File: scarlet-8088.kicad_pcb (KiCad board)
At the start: 2 copper layers, 0 parts

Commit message: Add grounded Mounting Holes to schematic
Signed-off-by: Lucy Mielke <user@domain.tld>
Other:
- board outline added: 305 x 244 mm
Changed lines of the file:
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@@
 		(legacy_teardrops no)
 	)
-	(paper "A4")
+	(paper "A2")
+	(title_block
+		(title "${TITLE}")
+		(date "${DATE}")
+		(rev "${REVISION}")
+		(company "${AUTHOR}")
+		(comment 1 "${COMMENT1}")
+	)
 	(layers
 		(0 "F.Cu" signal)
@@
 		(capping no)
 		(filling no)
-		(zone_defaults)
 		(pcbplotparams
 			(layerselection 0x00000000_00000000_55555555_5755f5ff)
@@
 		)
 	)
+	(property "AUTHOR" "Red Lucy Engineering")
+	(property "COMMENT1" "https://engineering.redlucy404.de")
+	(property "DATE" "${CURRENT_DATE}")
+	(property "REVISION" "1.0")
+	(property "TITLE" "\"scarlet-8088\" Intel-8088-based ATX Motherboard")
+	(gr_line
+		(start 147 99.5)
+		(end 147 343.5)
+		(stroke
+			(width 0.05)
+			(type default)
+		)
+		(layer "Edge.Cuts")
+	)
+	(gr_line
+		(start 147 99.5)
+		(end 452 99.5)
+		(stroke
+			(width 0.05)
+			(type default)
+		)
+		(layer "Edge.Cuts")
+	)
+	(gr_line
+		(start 147 343.5)
+		(end 452 343.5)
+		(stroke
+			(width 0.05)
+			(type default)
+		)
+		(layer "Edge.Cuts")
+	)
+	(gr_line
+		(start 452 343.5)
+		(end 452 99.5)
+		(stroke
+			(width 0.05)
+			(type default)
+		)
+		(layer "Edge.Cuts")
+	)
 	(embedded_fonts no)

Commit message: setup for JLCPCB 4-Layers
Signed-off-by: Lucy Mielke <user@domain.tld>
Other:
- copper layers 2 -> 4
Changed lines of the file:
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@@
 	(generator_version "10.0")
 	(general
-		(thickness 1.6)
+		(thickness 1.600198)
 		(legacy_teardrops no)
 	)
@@
 	)
 	(layers
-		(0 "F.Cu" signal)
-		(2 "B.Cu" signal)
-		(9 "F.Adhes" user "F.Adhesive")
-		(11 "B.Adhes" user "B.Adhesive")
+		(0 "F.Cu" signal "Front")
+		(4 "In1.Cu" signal)
+		(6 "In2.Cu" signal)
+		(2 "B.Cu" signal "Back")
 		(13 "F.Paste" user)
 		(15 "B.Paste" user)
-		(5 "F.SilkS" user "F.Silkscreen")
-		(7 "B.SilkS" user "B.Silkscreen")
+		(5 "F.SilkS" user)
+		(7 "B.SilkS" user)
 		(1 "F.Mask" user)
 		(3 "B.Mask" user)
-		(17 "Dwgs.User" user "User.Drawings")
-		(19 "Cmts.User" user "User.Comments")
-		(21 "Eco1.User" user "User.Eco1")
-		(23 "Eco2.User" user "User.Eco2")
 		(25 "Edge.Cuts" user)
 		(27 "Margin" user)
-		(31 "F.CrtYd" user "F.Courtyard")
-		(29 "B.CrtYd" user "B.Courtyard")
+		(31 "F.CrtYd" user)
+		(29 "B.CrtYd" user)
 		(35 "F.Fab" user)
-		(33 "B.Fab" user)
-		(39 "User.1" user)
-		(41 "User.2" user)
-		(43 "User.3" user)
-		(45 "User.4" user)
 	)
 	(setup
@@
 			(layer "dielectric 1"
 				(type "core")
-				(thickness 1.51)
+				(thickness 0.480066)
+				(material "FR4")
+				(epsilon_r 4.5)
+				(loss_tangent 0.02)
+			)
+			(layer "In1.Cu"
+				(type "copper")
+				(thickness 0.035)
+			)
+			(layer "dielectric 2"
+				(type "prepreg")
+				(thickness 0.480066)
+				(material "FR4")
+				(epsilon_r 4.5)
+				(loss_tangent 0.02)
+			)
+			(layer "In2.Cu"
+				(type "copper")
+				(thickness 0.035)
+			)
+			(layer "dielectric 3"
+				(type "core")
+				(thickness 0.480066)
 				(material "FR4")
 				(epsilon_r 4.5)
@@
 		)
 		(pad_to_mask_clearance 0)
+		(solder_mask_min_width 0.1016)
 		(allow_soldermask_bridges_in_footprints no)
 		(tenting
@@
 		(capping no)
 		(filling no)
+		(zone_defaults)
 		(pcbplotparams
 			(layerselection 0x00000000_00000000_55555555_5755f5ff)

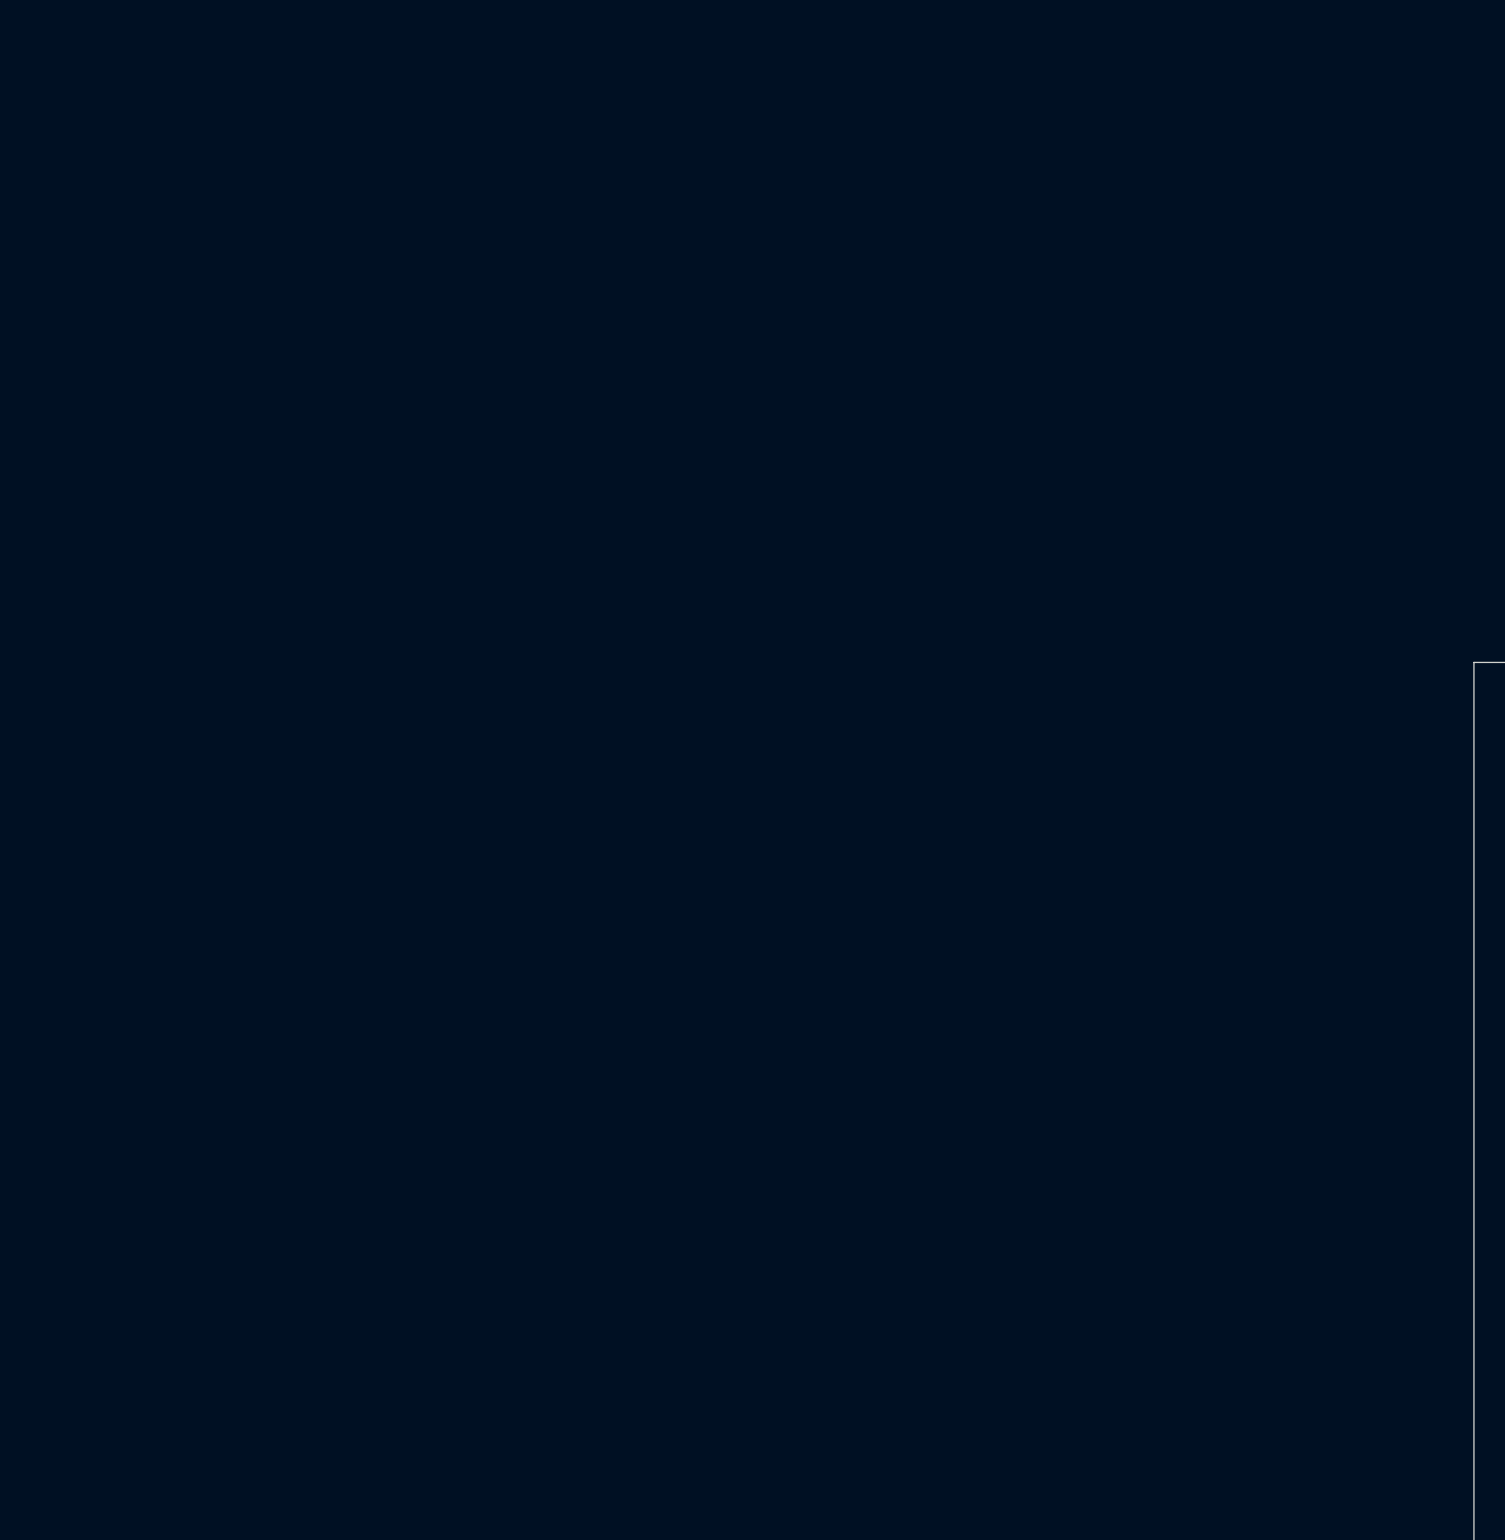
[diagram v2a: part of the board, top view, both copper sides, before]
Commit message: import all components into PCB editor
Signed-off-by: Lucy Mielke <user@domain.tld>
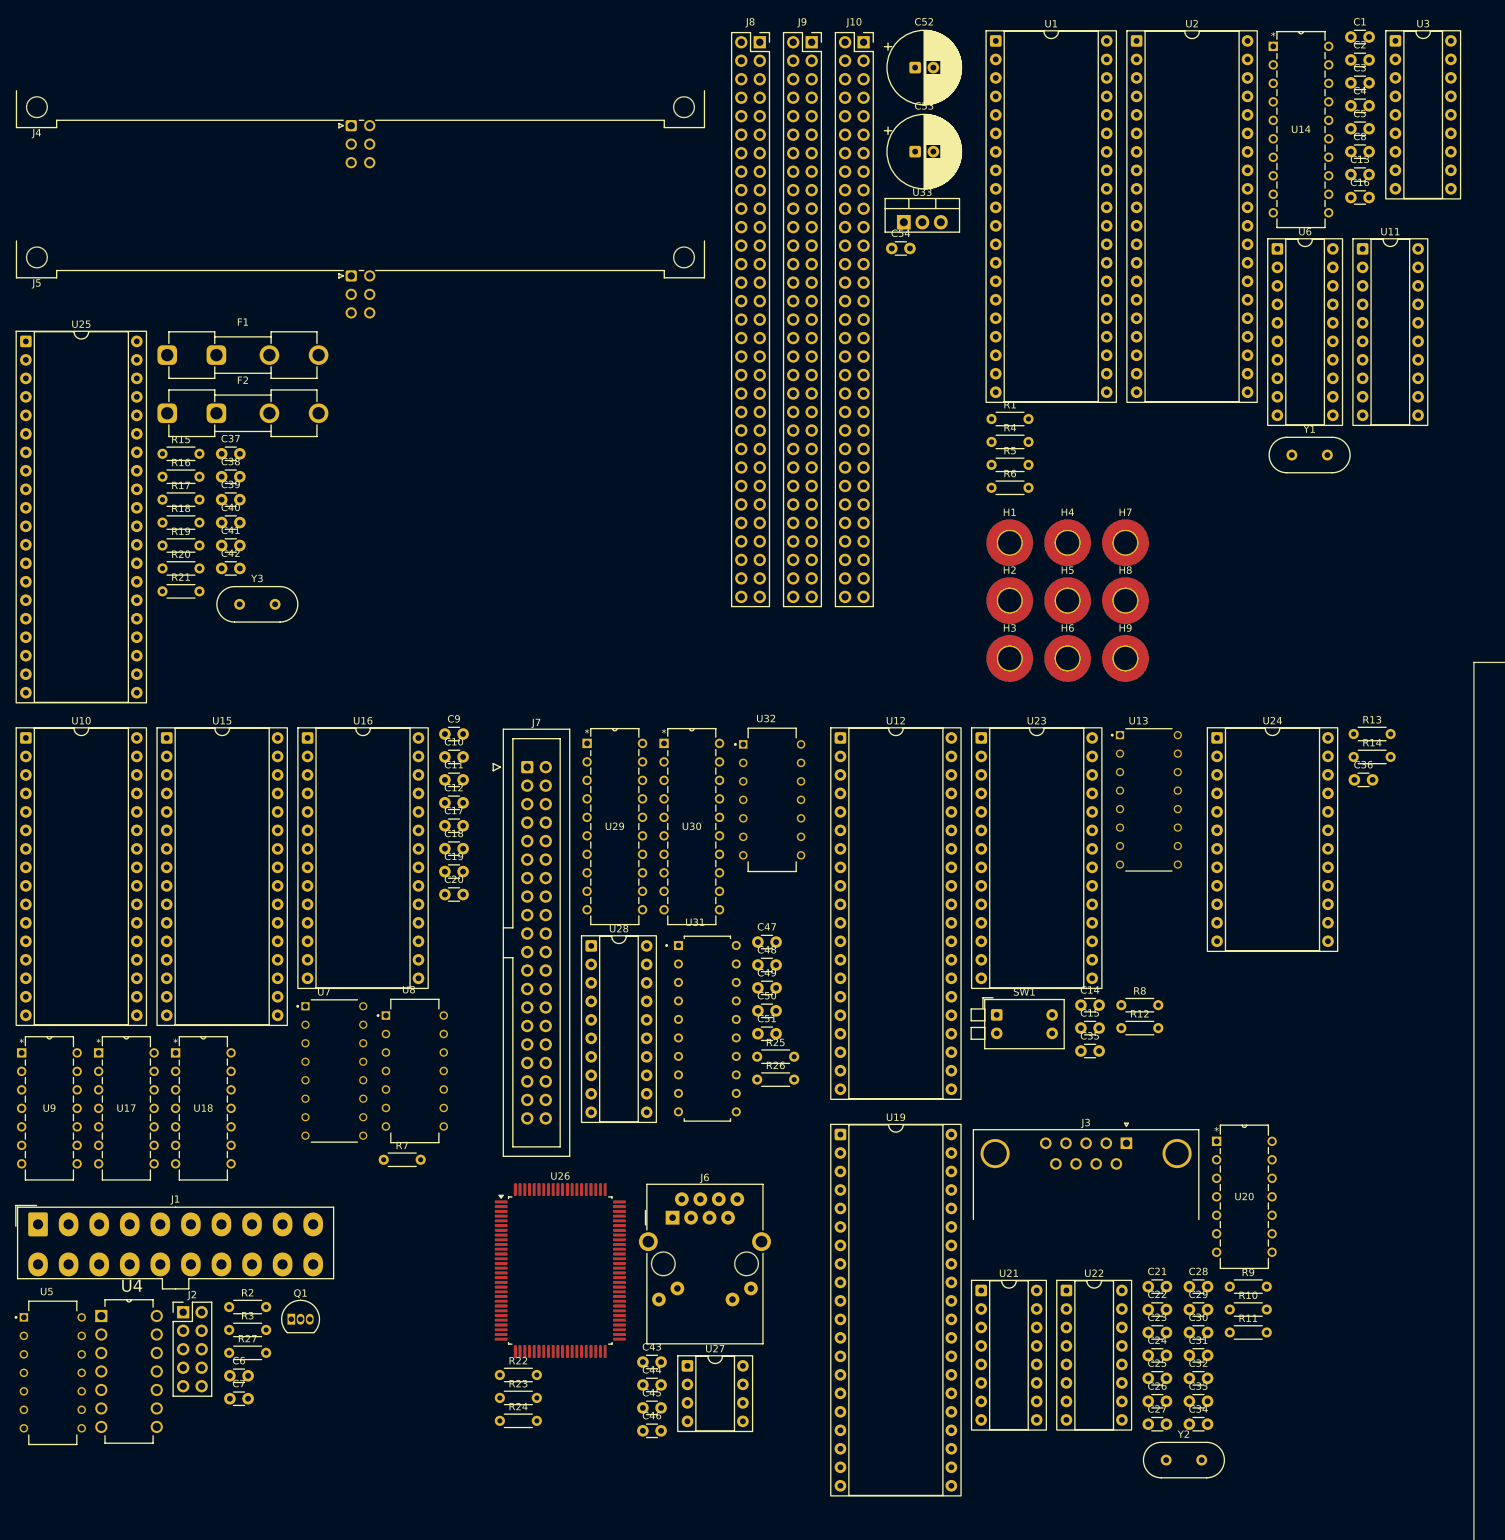
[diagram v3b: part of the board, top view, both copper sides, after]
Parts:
- added C1: 0.1uF, Capacitor_THT:C_Disc_D3.0mm_W1.6mm_P2.50mm, F.Cu at (130.1, 13.6)
- added C10: 0.1uF, Capacitor_THT:C_Disc_D3.0mm_W1.6mm_P2.50mm, F.Cu at (5.62, 112.5)
- added C11: 0.1uF, Capacitor_THT:C_Disc_D3.0mm_W1.6mm_P2.50mm, F.Cu at (5.62, 115.6)
- added C12: 0.1uF, Capacitor_THT:C_Disc_D3.0mm_W1.6mm_P2.50mm, F.Cu at (5.62, 118.8)
- added C13: 0.1uF, Capacitor_THT:C_Disc_D3.0mm_W1.6mm_P2.50mm, F.Cu at (130.1, 32.5)
- added C14: 0.1uF, Capacitor_THT:C_Disc_D3.0mm_W1.6mm_P2.50mm, F.Cu at (93.0, 146.6)
- added C15: 0.1uF, Capacitor_THT:C_Disc_D3.0mm_W1.6mm_P2.50mm, F.Cu at (93.0, 149.7)
- added C16: 0.1uF, Capacitor_THT:C_Disc_D3.0mm_W1.6mm_P2.50mm, F.Cu at (130.1, 35.6)
- added C17: 0.1uF, Capacitor_THT:C_Disc_D3.0mm_W1.6mm_P2.50mm, F.Cu at (5.62, 121.9)
- added C18: 0.1uF, Capacitor_THT:C_Disc_D3.0mm_W1.6mm_P2.50mm, F.Cu at (5.62, 125.1)
- added C19: 0.1uF, Capacitor_THT:C_Disc_D3.0mm_W1.6mm_P2.50mm, F.Cu at (5.62, 128.2)
- added C2: 0.1uF, Capacitor_THT:C_Disc_D3.0mm_W1.6mm_P2.50mm, F.Cu at (130.1, 16.7)
- added C20: 0.1uF, Capacitor_THT:C_Disc_D3.0mm_W1.6mm_P2.50mm, F.Cu at (5.62, 131.4)
- added C21: 0.1uF, Capacitor_THT:C_Disc_D3.0mm_W1.6mm_P2.50mm, F.Cu at (102.3, 185.3)
- added C22: 0.1uF, Capacitor_THT:C_Disc_D3.0mm_W1.6mm_P2.50mm, F.Cu at (102.3, 188.4)
- added C23: 20pF, Capacitor_THT:C_Disc_D3.0mm_W1.6mm_P2.50mm, F.Cu at (102.3, 191.6)
- added C24: 20pF, Capacitor_THT:C_Disc_D3.0mm_W1.6mm_P2.50mm, F.Cu at (102.3, 194.7)
- added C25: 0.1uF, Capacitor_THT:C_Disc_D3.0mm_W1.6mm_P2.50mm, F.Cu at (102.3, 197.9)
- added C26: 0.1uF, Capacitor_THT:C_Disc_D3.0mm_W1.6mm_P2.50mm, F.Cu at (102.3, 201.0)
- added C27: 1uF, Capacitor_THT:C_Disc_D3.0mm_W1.6mm_P2.50mm, F.Cu at (102.3, 204.2)
- added C28: 1uF, Capacitor_THT:C_Disc_D3.0mm_W1.6mm_P2.50mm, F.Cu at (107.9, 185.3)
- added C29: 1uF, Capacitor_THT:C_Disc_D3.0mm_W1.6mm_P2.50mm, F.Cu at (107.9, 188.4)
- added C3: 0.1uF, Capacitor_THT:C_Disc_D3.0mm_W1.6mm_P2.50mm, F.Cu at (130.1, 19.9)
- added C30: 1uF, Capacitor_THT:C_Disc_D3.0mm_W1.6mm_P2.50mm, F.Cu at (107.9, 191.6)
- added C31: 1uF, Capacitor_THT:C_Disc_D3.0mm_W1.6mm_P2.50mm, F.Cu at (107.9, 194.7)
- added C32: 1uF, Capacitor_THT:C_Disc_D3.0mm_W1.6mm_P2.50mm, F.Cu at (107.9, 197.9)
- added C33: 1uF, Capacitor_THT:C_Disc_D3.0mm_W1.6mm_P2.50mm, F.Cu at (107.9, 201.0)
- added C34: 1uF, Capacitor_THT:C_Disc_D3.0mm_W1.6mm_P2.50mm, F.Cu at (107.9, 204.2)
- added C35: 0.1uF, Capacitor_THT:C_Disc_D3.0mm_W1.6mm_P2.50mm, F.Cu at (93.0, 152.9)
- added C36: 0.1uF, Capacitor_THT:C_Disc_D3.0mm_W1.6mm_P2.50mm, F.Cu at (130.6, 115.6)
- added C37: 0.1uF, Capacitor_THT:C_Disc_D3.0mm_W1.6mm_P2.50mm, F.Cu at (-25.0, 70.8)
- added C38: 0.1uF, Capacitor_THT:C_Disc_D3.0mm_W1.6mm_P2.50mm, F.Cu at (-25.0, 74.0)
- added C39: 20pF, Capacitor_THT:C_Disc_D3.0mm_W1.6mm_P2.50mm, F.Cu at (-25.0, 77.1)
- added C4: 20pF, Capacitor_THT:C_Disc_D3.0mm_W1.6mm_P2.50mm, F.Cu at (130.1, 23.0)
- added C40: 20pF, Capacitor_THT:C_Disc_D3.0mm_W1.6mm_P2.50mm, F.Cu at (-25.0, 80.3)
- added C41: 0.1uF, Capacitor_THT:C_Disc_D3.0mm_W1.6mm_P2.50mm, F.Cu at (-25.0, 83.4)
- added C42: 0.1uF, Capacitor_THT:C_Disc_D3.0mm_W1.6mm_P2.50mm, F.Cu at (-25.0, 86.6)
- added C43: 0.1uF, Capacitor_THT:C_Disc_D3.0mm_W1.6mm_P2.50mm, F.Cu at (32.8, 195.6)
- added C44: 0.1uF, Capacitor_THT:C_Disc_D3.0mm_W1.6mm_P2.50mm, F.Cu at (32.8, 198.8)
- added C45: 0.1uF, Capacitor_THT:C_Disc_D3.0mm_W1.6mm_P2.50mm, F.Cu at (32.8, 201.9)
- added C46: 0.1uF, Capacitor_THT:C_Disc_D3.0mm_W1.6mm_P2.50mm, F.Cu at (32.8, 205.1)
- added C47: 0.1uF, Capacitor_THT:C_Disc_D3.0mm_W1.6mm_P2.50mm, F.Cu at (48.6, 137.9)
- added C48: 0.1uF, Capacitor_THT:C_Disc_D3.0mm_W1.6mm_P2.50mm, F.Cu at (48.6, 141.1)
- added C49: 0.1uF, Capacitor_THT:C_Disc_D3.0mm_W1.6mm_P2.50mm, F.Cu at (48.6, 144.2)
- added C5: 20pF, Capacitor_THT:C_Disc_D3.0mm_W1.6mm_P2.50mm, F.Cu at (130.1, 26.2)
- added C50: 0.1uF, Capacitor_THT:C_Disc_D3.0mm_W1.6mm_P2.50mm, F.Cu at (48.6, 147.4)
- added C51: 0.1uF, Capacitor_THT:C_Disc_D3.0mm_W1.6mm_P2.50mm, F.Cu at (48.6, 150.5)
- added C52: 2.2uF, Capacitor_THT:CP_Radial_D10.0mm_P2.50mm, F.Cu at (70.2, 17.8)
- added C53: 2.2uF, Capacitor_THT:CP_Radial_D10.0mm_P2.50mm, F.Cu at (70.2, 29.3)
- added C54: 0.1uF, Capacitor_THT:C_Disc_D3.0mm_W1.6mm_P2.50mm, F.Cu at (67.0, 42.6)
- added C6: 0.1uF, Capacitor_THT:C_Disc_D3.0mm_W1.6mm_P2.50mm, F.Cu at (-23.9, 197.5)
- added C7: 0.1uF, Capacitor_THT:C_Disc_D3.0mm_W1.6mm_P2.50mm, F.Cu at (-23.9, 200.7)
- added C8: 0.1uF, Capacitor_THT:C_Disc_D3.0mm_W1.6mm_P2.50mm, F.Cu at (130.1, 29.3)
- added C9: 0.1uF, Capacitor_THT:C_Disc_D3.0mm_W1.6mm_P2.50mm, F.Cu at (5.62, 109.3)
- added F1: Fuse, Fuse:Fuseholder_Clip-5x20mm_Eaton_1A5601-01_Inline_P20.80x6.76mm_D1.70mm_Horizontal, F.Cu at (-32.5, 57.3)
- added F2: Fuse, Fuse:Fuseholder_Clip-5x20mm_Eaton_1A5601-01_Inline_P20.80x6.76mm_D1.70mm_Horizontal, F.Cu at (-32.5, 65.3)
- added H1: MountingHole_Pad, MountingHole:MountingHole_3.2mm_M3_Pad_TopBottom, F.Cu at (83.2, 83.1)
- added H2: MountingHole_Pad, MountingHole:MountingHole_3.2mm_M3_Pad_TopBottom, F.Cu at (83.2, 91.0)
- added H3: MountingHole_Pad, MountingHole:MountingHole_3.2mm_M3_Pad_TopBottom, F.Cu at (83.2, 99.0)
- added H4: MountingHole_Pad, MountingHole:MountingHole_3.2mm_M3_Pad_TopBottom, F.Cu at (91.2, 83.1)
- added H5: MountingHole_Pad, MountingHole:MountingHole_3.2mm_M3_Pad_TopBottom, F.Cu at (91.2, 91.0)
- added H6: MountingHole_Pad, MountingHole:MountingHole_3.2mm_M3_Pad_TopBottom, F.Cu at (91.2, 99.0)
- added H7: MountingHole_Pad, MountingHole:MountingHole_3.2mm_M3_Pad_TopBottom, F.Cu at (99.1, 83.1)
- added H8: MountingHole_Pad, MountingHole:MountingHole_3.2mm_M3_Pad_TopBottom, F.Cu at (99.1, 91.0)
- added H9: MountingHole_Pad, MountingHole:MountingHole_3.2mm_M3_Pad_TopBottom, F.Cu at (99.1, 99.0)
- added J1: ATX-20, Connector_Molex:Molex_Mini-Fit_Jr_5566-20A_2x10_P4.20mm_Vertical, F.Cu at (-50.3, 176.7)
- added J10: Bus_ISA_8bit, Connector_PinSocket_2.54mm:PinSocket_2x31_P2.54mm_Vertical, F.Cu at (63.1, 14.3)
- added J2: F_PANEL, Connector_PinHeader_2.54mm:PinHeader_2x05_P2.54mm_Vertical, F.Cu at (-30.3, 188.8)
- added J3: DE-9SA-J4-2R, Connector_Dsub:DSUB-9_Socket_Horizontal_P2.77x2.84mm_EdgePinOffset7.70mm_Housed_MountingHolesOffset9.12mm, F.Cu at (99.3, 165.6)
- added J4: Mini-DIN-6 KBD, Connector_DIN:DIN41612_M-invers_3x2+10_Female_Horizontal_THT, F.Cu at (-45.3, 25.8)
- added J5: Mini-DIN-6 Mouse, Connector_DIN:DIN41612_M-invers_3x2+10_Female_Horizontal_THT, F.Cu at (-45.3, 46.4)
- added J6: RJ45_Amphenol_RJMG1BD3B8K1ANR, Connector_RJ:RJ45_Amphenol_RJMG1BD3B8K1ANR, F.Cu at (36.9, 175.8)
- added J7: Conn_02x20_Odd_Even, Connector_IDC:IDC-Header_2x20_P2.54mm_Vertical, F.Cu at (16.9, 113.9)
- added J8: Bus_ISA_8bit, Connector_PinSocket_2.54mm:PinSocket_2x31_P2.54mm_Vertical, F.Cu at (48.9, 14.3)
- added J9: Bus_ISA_8bit, Connector_PinSocket_2.54mm:PinSocket_2x31_P2.54mm_Vertical, F.Cu at (56.0, 14.3)
- added Q1: 2N7000, Package_TO_SOT_THT:TO-92_Inline, F.Cu at (-15.5, 189.7)
- added R1: 10k, Resistor_THT:R_Axial_DIN0204_L3.6mm_D1.6mm_P5.08mm_Horizontal, F.Cu at (80.7, 66.1)
- added R10: 10k, Resistor_THT:R_Axial_DIN0204_L3.6mm_D1.6mm_P5.08mm_Horizontal, F.Cu at (113.5, 188.4)
- added R11: 10k, Resistor_THT:R_Axial_DIN0204_L3.6mm_D1.6mm_P5.08mm_Horizontal, F.Cu at (113.5, 191.6)
- added R12: 10k, Resistor_THT:R_Axial_DIN0204_L3.6mm_D1.6mm_P5.08mm_Horizontal, F.Cu at (98.6, 149.7)
- added R13: 10k, Resistor_THT:R_Axial_DIN0204_L3.6mm_D1.6mm_P5.08mm_Horizontal, F.Cu at (130.5, 109.3)
- added R14: 10k, Resistor_THT:R_Axial_DIN0204_L3.6mm_D1.6mm_P5.08mm_Horizontal, F.Cu at (130.5, 112.5)
- added R15: 10k, Resistor_THT:R_Axial_DIN0204_L3.6mm_D1.6mm_P5.08mm_Horizontal, F.Cu at (-33.2, 70.8)
- added R16: 10k, Resistor_THT:R_Axial_DIN0204_L3.6mm_D1.6mm_P5.08mm_Horizontal, F.Cu at (-33.2, 74.0)
- added R17: 10k, Resistor_THT:R_Axial_DIN0204_L3.6mm_D1.6mm_P5.08mm_Horizontal, F.Cu at (-33.2, 77.1)
- added R18: 4,7k, Resistor_THT:R_Axial_DIN0204_L3.6mm_D1.6mm_P5.08mm_Horizontal, F.Cu at (-33.2, 80.3)
- added R19: 4,7k, Resistor_THT:R_Axial_DIN0204_L3.6mm_D1.6mm_P5.08mm_Horizontal, F.Cu at (-33.2, 83.4)
- added R2: 10k, Resistor_THT:R_Axial_DIN0204_L3.6mm_D1.6mm_P5.08mm_Horizontal, F.Cu at (-24.0, 188.1)
- added R20: 4,7k, Resistor_THT:R_Axial_DIN0204_L3.6mm_D1.6mm_P5.08mm_Horizontal, F.Cu at (-33.2, 86.6)
- added R21: 4,7k, Resistor_THT:R_Axial_DIN0204_L3.6mm_D1.6mm_P5.08mm_Horizontal, F.Cu at (-33.2, 89.7)
- added R22: 10k, Resistor_THT:R_Axial_DIN0204_L3.6mm_D1.6mm_P5.08mm_Horizontal, F.Cu at (13.2, 197.4)
- added R23: 3,3R, Resistor_THT:R_Axial_DIN0204_L3.6mm_D1.6mm_P5.08mm_Horizontal, F.Cu at (13.2, 200.5)
- added R24: 3,3R, Resistor_THT:R_Axial_DIN0204_L3.6mm_D1.6mm_P5.08mm_Horizontal, F.Cu at (13.2, 203.7)
- added R25: 10k, Resistor_THT:R_Axial_DIN0204_L3.6mm_D1.6mm_P5.08mm_Horizontal, F.Cu at (48.5, 153.7)
- added R26: 10k, Resistor_THT:R_Axial_DIN0204_L3.6mm_D1.6mm_P5.08mm_Horizontal, F.Cu at (48.5, 156.8)
- added R27: 3,3R, Resistor_THT:R_Axial_DIN0204_L3.6mm_D1.6mm_P5.08mm_Horizontal, F.Cu at (-24.0, 194.4)
- added R3: 10k, Resistor_THT:R_Axial_DIN0204_L3.6mm_D1.6mm_P5.08mm_Horizontal, F.Cu at (-24.0, 191.2)
- added R4: 10k, Resistor_THT:R_Axial_DIN0204_L3.6mm_D1.6mm_P5.08mm_Horizontal, F.Cu at (80.7, 69.2)
- added R5: 10k, Resistor_THT:R_Axial_DIN0204_L3.6mm_D1.6mm_P5.08mm_Horizontal, F.Cu at (80.7, 72.4)
- added R6: 10k, Resistor_THT:R_Axial_DIN0204_L3.6mm_D1.6mm_P5.08mm_Horizontal, F.Cu at (80.7, 75.5)
- added R7: 10k, Resistor_THT:R_Axial_DIN0204_L3.6mm_D1.6mm_P5.08mm_Horizontal, F.Cu at (-2.79, 167.8)
- added R8: 10k, Resistor_THT:R_Axial_DIN0204_L3.6mm_D1.6mm_P5.08mm_Horizontal, F.Cu at (98.6, 146.6)
- added R9: 10k, Resistor_THT:R_Axial_DIN0204_L3.6mm_D1.6mm_P5.08mm_Horizontal, F.Cu at (113.5, 185.3)
- added SW1: SW_DIP_x08, Button_Switch_THT:SW_DIP_SPSTx02_Piano_10.8x6.64mm_W7.62mm_P2.54mm, F.Cu at (81.4, 147.9)
- added U1: Intel_8088, Package_DIP:DIP-40_W15.24mm_Socket, F.Cu at (81.3, 14.1)
- added U10: AS6C4008-55PCN, Package_DIP:DIP-32_W15.24mm_Socket, F.Cu at (-51.9, 109.9)
- added U11: 74HCT373, Package_DIP:DIP-20_W7.62mm_Socket, F.Cu at (131.7, 42.7)
- added U12: 8255A, Package_DIP:DIP-40_W15.24mm_Socket, F.Cu at (60.0, 109.9)
- added U13: SN74HCT138N, SN74HCT138N Decoder/DEMUX:DIP794W45P254L1969H508Q16, F.Cu at (102.3, 118.4)
- added U14: SN74HCT245N, SN74HCT245N Transciever:SN74HCT245N, F.Cu at (127.0, 37.7)
- added U15: AS6C4008-55PCN, Package_DIP:DIP-32_W15.24mm_Socket, F.Cu at (-32.6, 109.9)
- added U16: 28C256, Package_DIP:DIP-28_W15.24mm_Socket, F.Cu at (-13.2, 109.9)
- added U17: CD74HCT14E, CD74HCT14E Inverter:CD74HCT14E, F.Cu at (-34.3, 168.4)
- added U18: CD74HCT10E, CD74HCT21E 4-Input AND-Gate:N14, F.Cu at (-23.8, 168.4)
- added U19: TL16C550BN, Package_DIP:DIP-40_W15.24mm_Socket, F.Cu at (60.0, 164.4)
- added U2: 8087, Package_DIP:DIP-40_W15.24mm_Socket, F.Cu at (100.7, 14.1)
- added U20: CD74HCT30E, footprints:N14, F.Cu at (119.3, 180.5)
- added U21: MAX232, Package_DIP:DIP-16_W7.62mm_Socket, F.Cu at (79.3, 185.8)
- added U22: MAX232, Package_DIP:DIP-16_W7.62mm_Socket, F.Cu at (91.0, 185.8)
- added U23: 8259A, Package_DIP:DIP-28_W15.24mm_Socket, F.Cu at (79.3, 109.9)
- added U24: 8254, Package_DIP:DIP-24_W15.24mm_Socket, F.Cu at (111.7, 109.9)
- added U25: Intel 8242, Package_DIP:DIP-40_W15.24mm_Socket, F.Cu at (-51.9, 55.4)
- added U26: Realtek RTL8019AS, Package_QFP:PQFP-100_14x20mm_P0.65mm, F.Cu at (21.5, 183.0)
- added U27: 93LCxxC, Package_DIP:DIP-8_W7.62mm_Socket, F.Cu at (38.9, 196.1)
- added U28: 74HCT688 (CD74HCT688E), Package_DIP:DIP-20_W7.62mm_Socket, F.Cu at (25.7, 138.4)
- added U29: SN74HCT245N, SN74HCT245N Transciever:SN74HCT245N, F.Cu at (32.8, 133.5)
- added U3: 8284, Package_DIP:DIP-18_W7.62mm_Socket, F.Cu at (136.2, 14.1)
- added U30: SN74HCT245N, SN74HCT245N Transciever:SN74HCT245N, F.Cu at (43.4, 133.5)
- added U31: SN74HCT573N, SN74HCT573N:DIP794W45P254L2540H508Q20, F.Cu at (41.7, 149.8)
- added U32: SN74HCT32N, SN74HCT32N:DIP794W45P254L1969H508Q14, F.Cu at (50.6, 118.4)
- added U33: L7905, Package_TO_SOT_THT:TO-220-3_Vertical, F.Cu at (68.7, 39.0)
- added U4: CD74HCT74E, CD74HCT74E D-Type Flip Flop:DIP254P762X508-14, F.Cu at (-34.0, 204.5)
- added U5: SN74HCT08N, SN74HCT08N AND-Gate IC:DIP794W45P254L1969H508Q14, F.Cu at (-48.2, 197.1)
- added U6: 8288, Package_DIP:DIP-20_W7.62mm_Socket, F.Cu at (120.0, 42.7)
- added U7: SN74HCT138N, SN74HCT138N Decoder/DEMUX:DIP794W45P254L1969H508Q16, F.Cu at (-9.56, 155.6)
- added U8: SN74HCT08N, SN74HCT08N AND-Gate IC:DIP794W45P254L1969H508Q14, F.Cu at (1.50, 155.6)
- added U9: CD74HCT21E, CD74HCT21E 4-Input AND-Gate:N14, F.Cu at (-44.9, 168.4)
- added Y1: 14.31818 MHz, Crystal:Crystal_HC49-U_Vertical, F.Cu at (122.0, 71.0)
- added Y2: 1.8432MHZ, Crystal:Crystal_HC49-U_Vertical, F.Cu at (104.7, 209.1)
- added Y3: 12MHz, Crystal:Crystal_HC49-U_Vertical, F.Cu at (-22.6, 91.5)

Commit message: Place mounting holes according to ATX spec
Signed-off-by: Lucy Mielke <user@domain.tld>
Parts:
- moved H9 420.2 mm to (445.4, 337.0)
- moved H6 391.1 mm to (445.4, 264.6)
- moved H3 363.8 mm to (445.5, 132.5)
- moved H8 310.1 mm to (288.0, 337.0)
- moved H5 262.4 mm to (288.0, 264.6)
- moved H7 262.0 mm to (163.5, 337.0)
- moved H2 205.6 mm to (288.0, 109.7)
- moved H4 195.4 mm to (163.5, 264.6)
- moved H1 84.6 mm to (163.5, 109.7)

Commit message: Add rear IO window markings according to ATX spec
Signed-off-by: Lucy Mielke <user@domain.tld>
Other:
- board text added: "REAR IO WINDOW"
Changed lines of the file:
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@@
 		(layer "Edge.Cuts")
+	)
+	(gr_rect
+		(start 295.49 95.45)
+		(end 454.25 110.3)
+		(stroke
+			(width 0.1)
+			(type solid)
+		)
+		(fill reverse_hatch)
+		(layer "F.Fab")
+	)
+	(gr_text "REAR IO WINDOW"
+		(at 374.87 102.875 0)
+		(layer "F.Fab")
+		(effects
+			(font
+				(size 1 1)
+				(thickness 0.15)
+			)
+			(justify bottom)
+		)
 	)
 	(dimension
@@
 		(layer "F.Fab")
 		(pts
+			(xy 163.51 109.65) (xy 295.49 109.69)
+		)
+		(height -31.47)
+		(orientation 0)
+		(format
+			(prefix "")
+			(suffix "")
+			(units 3)
+			(units_format 0)
+			(precision 4)
+			(suppress_zeroes yes)
+		)
+		(style
+			(thickness 0.1)
+			(arrow_length 1.27)
+			(text_position_mode 0)
+			(arrow_direction outward)
+			(extension_height 0.58642)
+			(extension_offset 0.5)
+			(keep_text_aligned yes)
+		)
+		(gr_text "131,98"
+			(at 229.5 77.03 0)
+			(layer "F.Fab")
+			(effects
+				(font
+					(size 1 1)
+					(thickness 0.15)
+				)
+			)
+		)
+	)
+	(dimension
+		(type orthogonal)
+		(layer "F.Fab")
+		(pts
 			(xy 163.51 99.49) (xy 287.96 99.49)
 		)
@@
 			(layer "F.Fab")
 			(effects
+				(font
+					(size 1 1)
+					(thickness 0.15)
+				)
+			)
+		)
+	)
+	(dimension
+		(type orthogonal)
+		(layer "F.Fab")
+		(pts
+			(xy 295.49 109.69) (xy 454.25 110.3)
+		)
+		(height -18.87)
+		(orientation 0)
+		(format
+			(prefix "")
+			(suffix "")
+			(units 3)
+			(units_format 0)
+			(precision 4)
+			(suppress_zeroes yes)
+		)
+		(style
+			(thickness 0.1)
+			(arrow_length 1.27)
+			(text_position_mode 0)
+			(arrow_direction outward)
+			(extension_height 0.58642)
+			(extension_offset 0.5)
+			(keep_text_aligned yes)
+		)
+		(gr_text "158,76"
+			(at 374.87 89.67 0)
+			(layer "F.Fab")
+			(effects

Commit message: change Mini-DIN-6 Footprint; Place ISA slots correctly
Signed-off-by: Lucy Mielke <user@domain.tld>
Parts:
- J4, J5: footprint Connector_DIN:DIN41612_M-invers_3x2+10_Female_Horizontal_THT -> minidin_6_ps2_pcb_mount:minidin_6_ps2_pcb_mount
- SW1: footprint Button_Switch_THT:SW_DIP_SPSTx02_Piano_10.8x6.64mm_W7.62mm_P2.54mm -> Button_Switch_THT:SW_DIP_SPSTx08_Piano_10.8x21.88mm_W7.62mm_P2.54mm
- moved J4 486.7 mm to (434.8, 105.8)
- moved J5 464.0 mm to (414.9, 105.8)
- moved J3 288.9 mm to (383.0, 111.0), turned to 180 degrees
- moved SW1 187.4 mm to (268.3, 134.8)
- moved J10 187.2 mm to (214.3, 124.8)
- moved J9 176.8 mm to (194.0, 124.9)
- moved J8 166.8 mm to (173.7, 124.9)

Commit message: initial component layout (and fresh schematic export)
Signed-off-by: Lucy Mielke <user@domain.tld>
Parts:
- moved U5 493.9 mm to (432.1, 311.7), turned to -90 degrees
- moved C7 481.3 mm to (443.5, 315.5), turned to 90 degrees
- moved F2 476.1 mm to (438.2, 136.7), turned to 90 degrees
- moved R2 474.8 mm to (437.2, 300.7), turned to -90 degrees
- moved R19 461.3 mm to (426.8, 118.4)
- moved J1 459.8 mm to (382.4, 332.5), turned to 180 degrees
- moved R18 459.3 mm to (424.8, 115.4)
- moved C42 458.7 mm to (431.8, 127.1), turned to 90 degrees
- moved F1 457.4 mm to (418.0, 136.2), turned to 90 degrees
- moved C6 452.8 mm to (413.9, 312.9), turned to -90 degrees
- moved R3 446.1 mm to (408.2, 301.8), turned to 180 degrees
- moved R21 442.1 mm to (408.0, 118.3)
- moved U4 441.0 mm to (392.8, 315.5), turned to -90 degrees
- moved R20 440.3 mm to (406.2, 115.1)
- moved C41 438.3 mm to (411.1, 126.3), turned to 90 degrees
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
